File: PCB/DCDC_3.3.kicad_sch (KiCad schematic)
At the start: 21 parts, among them U10 HT75xx-1-SOT89, U11 LV2842XLVDDCR

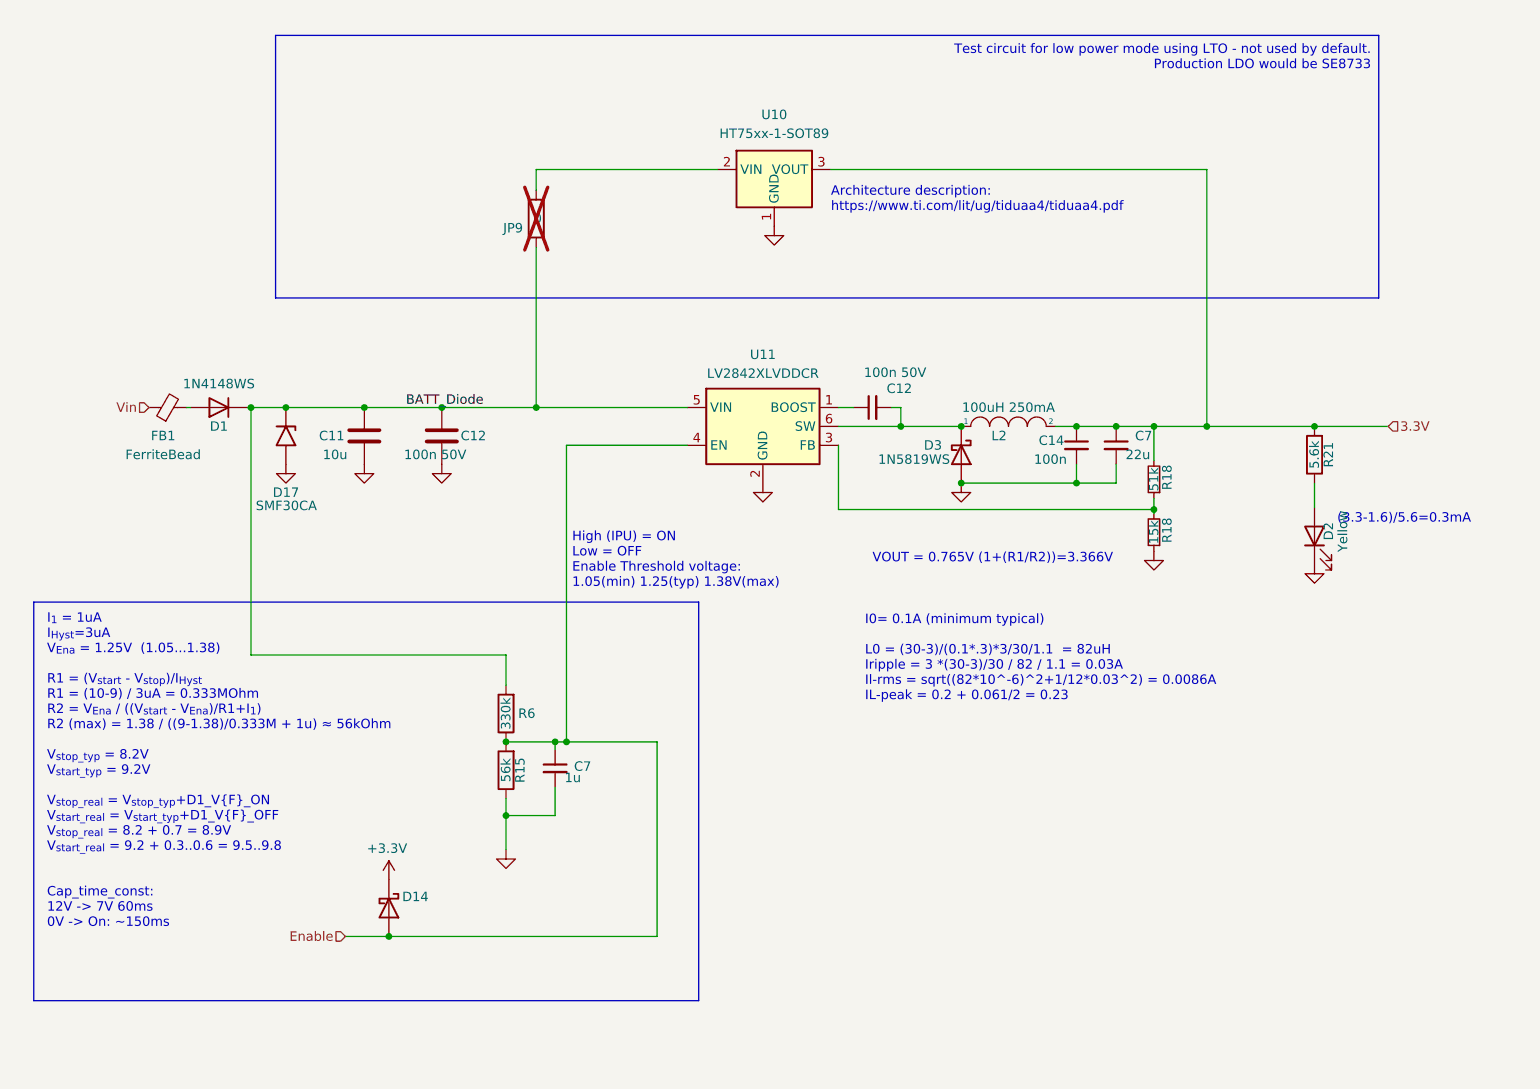
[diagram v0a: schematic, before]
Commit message: Removed diode and a resistor - fixes DCDC SHDN pin. Corrected SHDN pin voltage calculation based on real threshold value
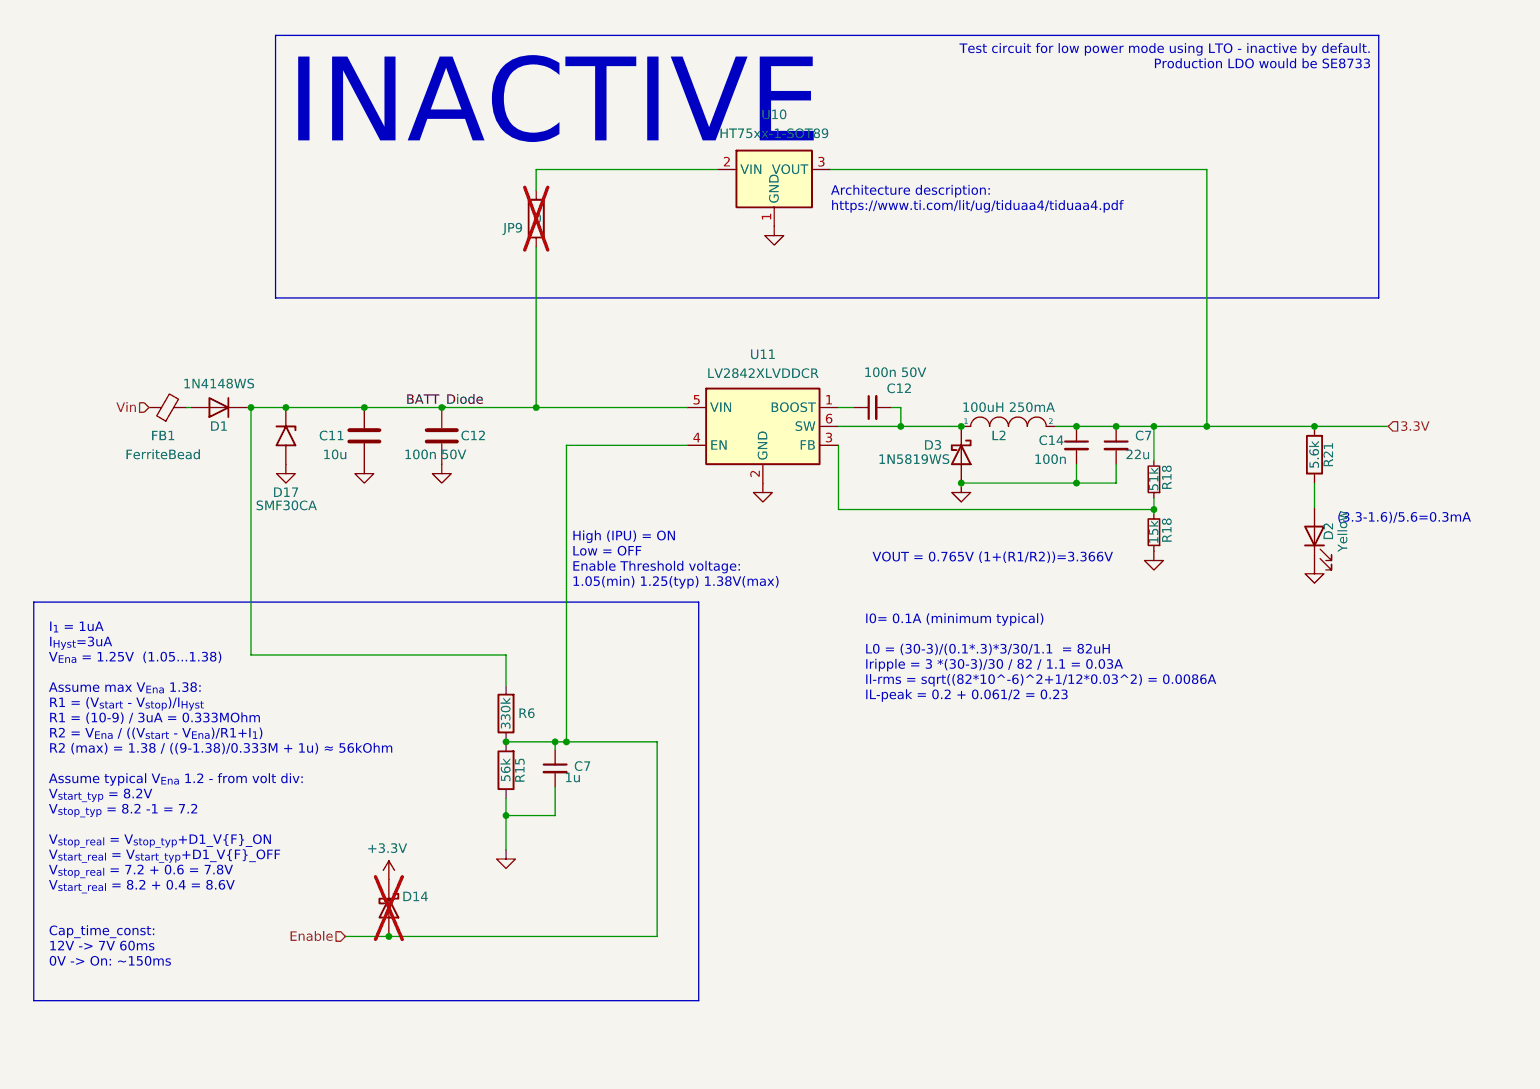
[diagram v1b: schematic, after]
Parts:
- D14: now not fitted
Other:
- note added: "INACTIVE"
- note added: "I_{1} = 1uA I_{Hyst}=3uA V_{Ena} = 1.25V (1.05...1.38) Assume max V_{Ena} 1.38: R1 = (V_{start} - V_{stop})/I_{Hyst} R1 = (10-9) / 3uA = 0.333MOhm R2 = V_{Ena} / ((V_{start} - V_{Ena})/R1+I_{1}) R2 (max) = 1.38 / ((9-1.38)/0.333M + 1u) ≈ 56kOhm Assume typical V_{Ena} 1.2 - from volt div: V_{start_typ} = 8.2V V_{stop_typ} = 8.2 -1 = 7.2 V_{stop_real} = V_{stop_typ}+D1_V{F}_ON V_{start_real} = V_{s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"
- note removed: "I_{1} = 1uA I_{Hyst}=3uA V_{Ena} = 1.25V (1.05...1.38) R1 = (V_{start} - V_{stop})/I_{Hyst} R1 = (10-9) / 3uA = 0.333MOhm R2 = V_{Ena} / ((V_{start} - V_{Ena})/R1+I_{1}) R2 (max) = 1.38 / ((9-1.38)/0.333M + 1u) ≈ 56kOhm V_{stop_typ} = 8.2V V_{start_typ} = 9.2V V_{stop_real} = V_{stop_typ}+D1_V{F}_ON V_{start_real} = V_{start_typ}+D1_V{F}_OFF V_{stop_real} = 8.2 + 0.7 = 8.9V V_{start_real} = 9.2 +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"
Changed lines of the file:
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@@
     (fill (type none))
   )
-  (text_box "Test circuit for low power mode using LTO - not used by default.\nProduction LDO would be SE8733"
+  (text_box "Test circuit for low power mode using LTO - inactive by default.\nProduction LDO would be SE8733"
     (at 70.612 29.972 0) (size 148.336 35.306)
     (stroke (width 0) (type default))
@@
     (effects (font (size 1.27 1.27)) (justify left bottom))
   )
-  (text "I_{1} = 1uA\nI_{Hyst}=3uA\nV_{Ena} = 1.25V  (1.05...1.38)\n\nR1 = (V_{start} - V_{stop})/I_{Hyst}\nR1 = (10-9) / 3uA = 0.333MOhm\nR2 = V_{Ena} / ((V_{start} - V_{Ena})/R1+I_{1})\nR2 (max) = 1.38 / ((9-1.38)/0.333M + 1u) ≈ 56kOhm\n\nV_{stop_typ} = 8.2V\nV_{start_typ} = 9.2V\n\nV_{stop_real} = V_{stop_typ}+D1_V{F}_ON\nV_{start_real} = V_{start_typ}+D1_V{F}_OFF\nV_{stop_real} = 8.2 + 0.7 = 8.9V\nV_{start_real} = 9.2 + 0.3..0.6 = 9.5..9.8\n\n\nCap_time_const:\n12V -> 7V 60ms\n0V -> On: ~150ms"
-    (at 39.878 150.114 0)
+  (text "I_{1} = 1uA\nI_{Hyst}=3uA\nV_{Ena} = 1.25V  (1.05...1.38)\n\nAssume max V_{Ena} 1.38:\nR1 = (V_{start} - V_{stop})/I_{Hyst}\nR1 = (10-9) / 3uA = 0.333MOhm\nR2 = V_{Ena} / ((V_{start} - V_{Ena})/R1+I_{1})\nR2 (max) = 1.38 / ((9-1.38)/0.333M + 1u) ≈ 56kOhm\n\nAssume typical V_{Ena} 1.2 - from volt div:\nV_{start_typ} = 8.2V\nV_{stop_typ} = 8.2 -1 = 7.2\n\nV_{stop_real} = V_{stop_typ}+D1_V{F}_ON\nV_{start_real} = V_{start_typ}+D1_V{F}_OFF\nV_{stop_real} = 7.2 + 0.6 = 7.8V\nV_{start_real} = 8.2 + 0.4 = 8.6V\n\n\nCap_time_const:\n12V -> 7V 60ms\n0V -> On: ~150ms"
+    (at 40.132 155.448 0)
     (effects (font (size 1.27 1.27)) (justify left bottom) (href "https://everycircuit.com/circuit/6478510418558976"))
   )
@@
     (at 110.49 104.394 0)
     (effects (font (size 1.27 1.27)) (justify left bottom))
+  )
+  (text "INACTIVE" (at 72.136 45.72 0)
+    (effects (font (size 11.27 11.27)) (justify left bottom))
   )
   (text "VOUT = 0.765V (1+(R1/R2))=3.366V" (at 150.876 101.092 0)
@@
   )
   (symbol (lib_id "Diode:1N5819") (at 85.852 147.32 270) (unit 1)
-    (in_bom yes) (on_board yes) (dnp no)
+    (in_bom yes) (on_board yes) (dnp yes)
     (property "Reference" "D14" (at 89.408 145.796 90)
       (effects (font (size 1.27 1.27)))
